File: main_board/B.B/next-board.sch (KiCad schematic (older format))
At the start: 6 parts

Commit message: preparation_to_drawing_PCB
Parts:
- removed Q?: Q_NMOS_DSG, symbol Device:Q_NMOS_DSG
- added Q?: CJ3134K, Package_TO_SOT_SMD:SOT-23, symbol Transistor_FET:2N7002
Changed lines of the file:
@@
 F3 "DIN" I L 8650 3550 50
 $EndSheet
-$Comp
-L Device:Q_NMOS_DSG Q?
-U 1 1 5FAB2954
-P 8150 3450
-AR Path="/5F9EE529/5FAB2954" Ref="Q?"  Part="1"
-AR Path="/5FA9DBB3/5FAB2954" Ref="Q?"  Part="1"
-AR Path="/5FA9675D/5FAA484F/5FAB2954" Ref="Q?"  Part="1"
-AR Path="/5FA9675D/5FAB2954" Ref="Q?"  Part="1"
-F 0 "Q?" H 8354 3496 50  0000 L CNN
-F 1 "Q_NMOS_DSG" H 8354 3405 50  0000 L CNN
-F 2 "" H 8350 3550 50  0001 C CNN
-F 3 "~" H 8150 3450 50  0001 C CNN
-	1    8150 3450
-	0    1    1    0
-$EndComp
 Text HLabel 7800 3550 0    50   Input ~ 0
 WS2812
@@
 	1    0    0    -1
 $EndComp
+$Comp
+L Transistor_FET:2N7002 Q?
+U 1 1 5FAB1240
+P 8150 3450
+AR Path="/5F77B818/5FAB1240" Ref="Q?"  Part="1"
+AR Path="/5FA9675D/5FAB1240" Ref="Q?"  Part="1"
+F 0 "Q?" H 8354 3496 50  0000 L CNN
+F 1 "CJ3134K" H 8354 3405 50  0000 L CNN
+F 2 "Package_TO_SOT_SMD:SOT-23" H 8350 3375 50  0001 L CIN
+F 3 "https://datasheet.lcsc.com/szlcsc/Changjiang-Electronics-Tech-CJ-CJ3134K_C110100.pdf" H 8150 3450 50  0001 L CNN
+F 4 "C110100" H 8150 3450 50  0001 C CNN "LCSC"
+F 5 "nutno vyměnit (musí být ->  Vgs-min>1.6V)" H 8150 3450 50  0001 C CNN "poznamka"
+	1    8150 3450
+	0    1    1    0
+$EndComp
 $EndSCHEMATC

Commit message: complete_preparation_to_drawing_PCB
footprint for all component and LCSC code for everything for mounting in JLCPCB
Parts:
- C112: renamed from C?; footprint (none) -> Capacitor_SMD:C_0402_1005Metric
- R40: renamed from R?; footprint (none) -> Resistor_SMD:R_0402_1005Metric
- gave numbers to parts that had none: 4
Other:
- moved on the sheet: C112, L3
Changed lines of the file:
@@
 $EndDescr
 $Comp
-L B.B-eagle-import:GND #GND?
+L B.B-eagle-import:GND #GND0131
 U 1 1 5FA986E8
 P 3400 4350
-F 0 "#GND?" H 3400 4350 50  0001 C CNN
+F 0 "#GND0131" H 3400 4350 50  0001 C CNN
 F 1 "GND" H 3400 4270 59  0000 C CNN
 F 2 "" H 3400 4350 50  0001 C CNN
@@
 $EndComp
 $Comp
-L B.B-eagle-import:GND #GND?
+L B.B-eagle-import:GND #GND0130
 U 1 1 5FA9899C
 P 2850 4200
-F 0 "#GND?" H 2850 4200 50  0001 C CNN
+F 0 "#GND0130" H 2850 4200 50  0001 C CNN
 F 1 "GND" H 2850 4120 59  0000 C CNN
 F 2 "" H 2850 4200 50  0001 C CNN
@@
 SHUTDOWN
 $Comp
-L B.B-rescue:LDC1314 U?
+L B.B-rescue:LDC1314 U66
 U 1 1 5FA9CA7D
 P 3400 3450
-F 0 "U?" H 3400 4325 50  0000 C CNN
+F 0 "U66" H 3400 4325 50  0000 C CNN
 F 1 "LDC1314" H 3400 4234 50  0000 C CNN
 F 2 "Package_DFN_QFN:WQFN-16-1EP_4x4mm_P0.5mm_EP2.6x2.6mm_ThermalVias" H 3400 4200 50  0001 C CNN
@@
 	8400 3550 8650 3550
 Connection ~ 8400 3550
-$Comp
-L Device:L L?
-U 1 1 60038722
-P 4200 2950
-F 0 "L?" V 4250 2850 50  0000 C CNN
-F 1 "L" V 4250 3000 50  0000 C CNN
-F 2 "" H 4200 2950 50  0001 C CNN
-F 3 "~" H 4200 2950 50  0001 C CNN
-	1    4200 2950
-	0    -1   -1   0
-$EndComp
-$Comp
-L Device:C C?
-U 1 1 6003A0BB
-P 4200 3050
-F 0 "C?" V 4150 2950 50  0000 C CNN
-F 1 "C" V 4150 3150 50  0000 C CNN
-F 2 "" H 4238 2900 50  0001 C CNN
-F 3 "~" H 4200 3050 50  0001 C CNN
-	1    4200 3050
-	0    1    1    0
-$EndComp
-Wire Wire Line
-	4000 3050 4000 2950
-Wire Wire Line
-	4000 2950 4050 2950
-Wire Wire Line
-	4000 3050 4050 3050
-Wire Wire Line
-	4350 2950 4400 2950
-Wire Wire Line
-	4400 2950 4400 3050
-Wire Wire Line
-	4400 3050 4350 3050
-Wire Wire Line
-	4400 3050 4400 3150
-Connection ~ 4400 3050
+Wire Wire Line
+	4500 3050 4500 3150
+Connection ~ 4500 3050
 Wire Wire Line
 	3900 3050 4000 3050
 Connection ~ 4000 3050
 Wire Wire Line
-	3900 3150 4400 3150
-Wire Wire Line
-	4000 3350 4000 3250
-Wire Wire Line
-	4000 3250 4050 3250
-Wire Wire Line
-	4000 3350 4050 3350
-Wire Wire Line
-	4350 3250 4400 3250
-Wire Wire Line
-	4400 3250 4400 3350
-Wire Wire Line
-	4400 3350 4350 3350
-Wire Wire Line
-	4400 3350 4400 3450
-Connection ~ 4400 3350
-Wire Wire Line
-	3900 3350 4000 3350
-Connection ~ 4000 3350
-Wire Wire Line
-	3900 3450 4400 3450
-Wire Wire Line
-	4000 3650 4000 3550
-Wire Wire Line
-	4000 3550 4050 3550
-Wire Wire Line
-	4000 3650 4050 3650
-Wire Wire Line
-	4350 3550 4400 3550
-Wire Wire Line
-	4400 3550 4400 3650
-Wire Wire Line
-	4400 3650 4350 3650
-Wire Wire Line
-	4400 3650 4400 3750
-Connection ~ 4400 3650
-Wire Wire Line
-	3900 3650 4000 3650
-Connection ~ 4000 3650
-Wire Wire Line
-	3900 3750 4400 3750
-Wire Wire Line
-	4000 3950 4000 3850
-Wire Wire Line
-	4000 3850 4050 3850
-Wire Wire Line
-	4000 3950 4050 3950
-Wire Wire Line
-	4350 3850 4400 3850
-Wire Wire Line
-	4400 3850 4400 3950
-Wire Wire Line
-	4400 3950 4350 3950
-Wire Wire Line
-	4400 3950 4400 4050
-Connection ~ 4400 3950
-Wire Wire Line
-	3900 3950 4000 3950
-Connection ~ 4000 3950
-Wire Wire Line
-	3900 4050 4400 4050
-$Comp
-L Device:R R?
+	3900 3150 4500 3150
+$Comp
+L Device:R R40
 U 1 1 60083558
 P 8400 3350
-F 0 "R?" H 8470 3396 50  0000 L CNN
+F 0 "R40" H 8470 3396 50  0000 L CNN
 F 1 "12k" H 8470 3305 50  0000 L CNN
-F 2 "" V 8330 3350 50  0001 C CNN
+F 2 "Resistor_SMD:R_0402_1005Metric" V 8330 3350 50  0001 C CNN
 F 3 "~" H 8400 3350 50  0001 C CNN
 F 4 "C25752" H 8400 3350 50  0001 C CNN "LCSC"
@@
 $EndComp
 $Comp
-L Device:R R?
+L Device:R R39
 U 1 1 5FAB4344
 P 7850 3350
-F 0 "R?" H 7920 3396 50  0000 L CNN
+F 0 "R39" H 7920 3396 50  0000 L CNN
 F 1 "12k" H 7920 3305 50  0000 L CNN
 F 2 "Resistor_SMD:R_0402_1005Metric" V 7780 3350 50  0001 C CNN
@@
 P 8150 3450
 AR Path="/5F77B818/5FAB1240" Ref="Q?"  Part="1"
-AR Path="/5FA9675D/5FAB1240" Ref="Q?"  Part="1"
-F 0 "Q?" H 8354 3496 50  0000 L CNN
+AR Path="/5FA9675D/5FAB1240" Ref="Q6"  Part="1"
+F 0 "Q6" H 8354 3496 50  0000 L CNN
 F 1 "CJ3134K" H 8354 3405 50  0000 L CNN
 F 2 "Package_TO_SOT_SMD:SOT-23" H 8350 3375 50  0001 L CIN
@@
 	0    1    1    0
 $EndComp
+Wire Wire Line
+	4500 2950 4500 3050
+Wire Wire Line
+	4000 3050 4000 2950
+Wire Wire Line
+	4450 2950 4500 2950
+Wire Wire Line
+	4000 2950 4150 2950
+$Comp
+L Device:L L3
+U 1 1 60038722
+P 4300 2950
+F 0 "L3" V 4350 2800 50  0000 C CNN
+F 1 "L" V 4350 3100 50  0000 C CNN
+F 2 "" H 4300 2950 50  0001 C CNN
+F 3 "~" H 4300 2950 50  0001 C CNN
+	1    4300 2950
+	0    -1   -1   0
+$EndComp
+Wire Wire Line
+	4000 3050 4150 3050
+Wire Wire Line
+	4500 3050 4450 3050
+$Comp
+L Device:C C112
+U 1 1 6003A0BB
+P 4300 3050
+F 0 "C112" V 4250 2900 50  0000 C CNN
+F 1 "C" V 4250 3150 50  0000 C CNN
+F 2 "Capacitor_SMD:C_0402_1005Metric" H 4338 2900 50  0001 C CNN
+F 3 "~" H 4300 3050 50  0001 C CNN
+	1    4300 3050
+	0    1    1    0
+$EndComp
+Wire Wire Line
+	3900 3350 4000 3350
+Connection ~ 4000 3350
+Wire Wire Line
+	3900 3450 4500 3450
+Wire Wire Line
+	4000 3350 4000 3250
+Wire Wire Line
+	4000 3250 4150 3250
+Wire Wire Line
+	4000 3350 4150 3350
+Wire Wire Line
+	3900 3650 4000 3650
+Connection ~ 4000 3650
+Wire Wire Line
+	3900 3750 4500 3750
+Wire Wire Line
+	4000 3650 4000 3550
+Wire Wire Line
+	4000 3550 4150 3550
+Wire Wire Line
+	4000 3650 4150 3650
+Wire Wire Line
+	3900 3950 4000 3950
+Connection ~ 4000 3950
+Wire Wire Line
+	3900 4050 4500 4050
+Wire Wire Line
+	4000 3950 4000 3850
+Wire Wire Line
+	4000 3850 4150 3850
+Wire Wire Line
+	4000 3950 4150 3950
+Wire Wire Line
+	4500 3350 4500 3450
+Connection ~ 4500 3350
+Wire Wire Line
+	4500 3250 4500 3350
+Wire Wire Line
+	4450 3250 4500 3250
+Wire Wire Line
+	4500 3350 4450 3350
+Wire Wire Line
+	4500 3650 4500 3750
+Connection ~ 4500 3650
+Wire Wire Line
+	4500 3550 4500 3650
+Wire Wire Line
+	4450 3550 4500 3550
+Wire Wire Line
+	4500 3650 4450 3650
+Wire Wire Line
+	4500 3950 4500 4050
+Connection ~ 4500 3950
+Wire Wire Line
+	4500 3850 4500 3950
+Wire Wire Line
+	4450 3850 4500 3850
+Wire Wire Line
+	4500 3950 4450 3950
 $EndSCHEMATC

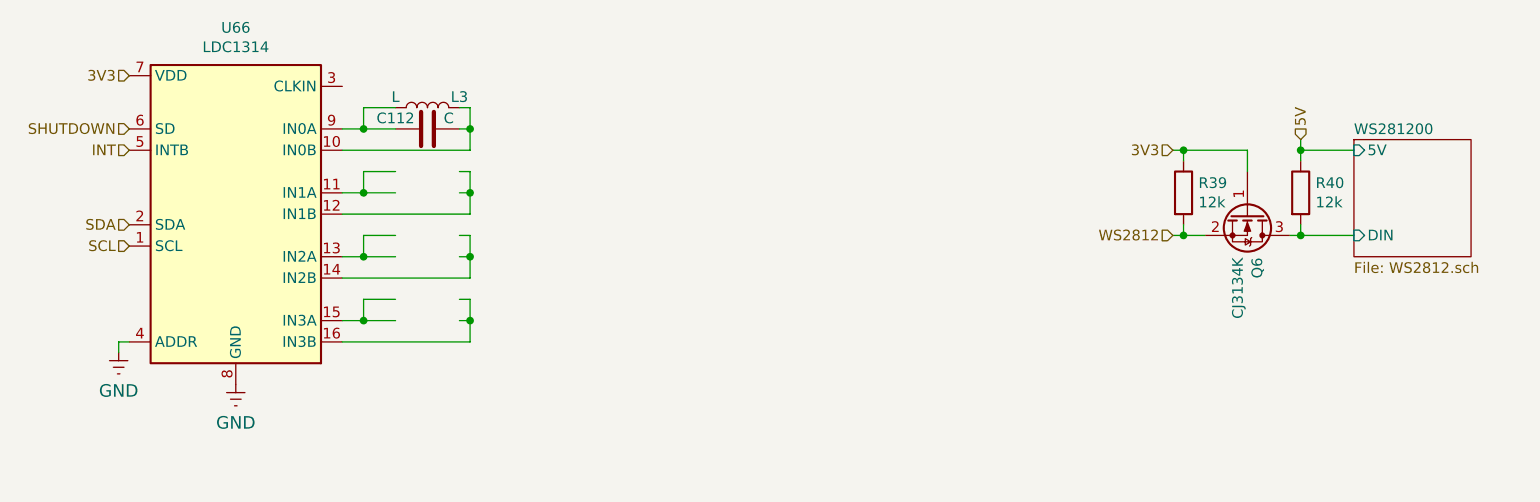
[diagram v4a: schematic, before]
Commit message: orezavani
smazaní A9G, SD karty, a zvuku
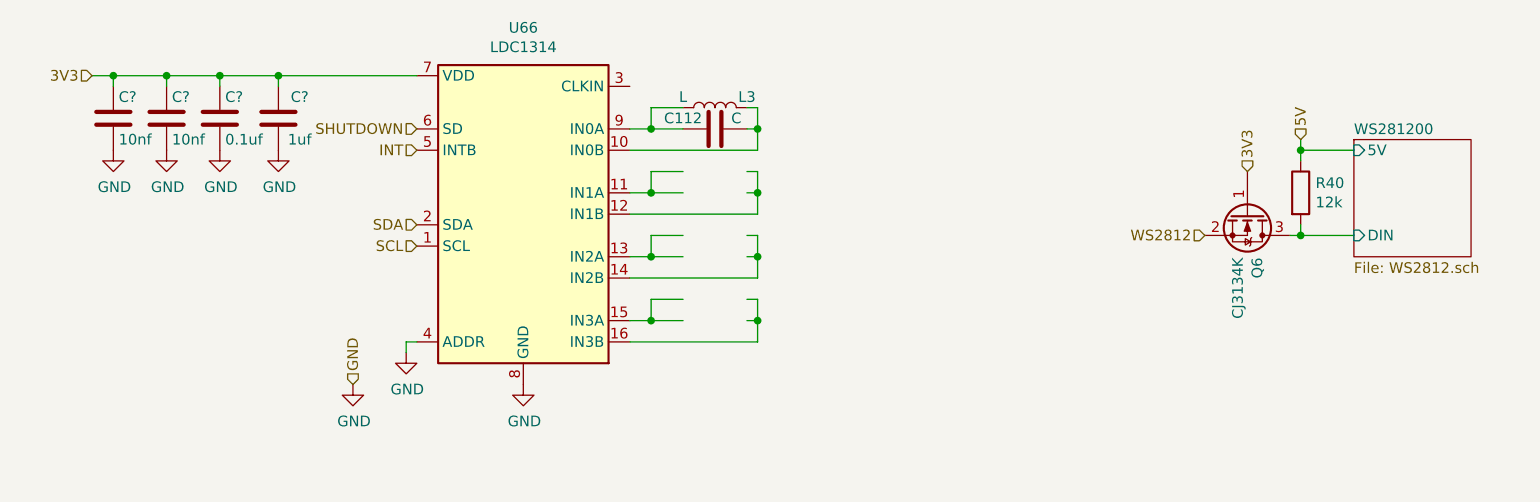
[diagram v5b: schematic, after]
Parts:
- removed R39: 12k, Resistor_SMD:R_0402_1005Metric, symbol Device:R
- added C?: 1uf, Capacitor_SMD:C_0402_1005Metric, symbol Device:C
- added C?: 0.1uf, Resistor_SMD:R_0402_1005Metric, symbol Device:C
- added C? (x2): 10nf, Capacitor_SMD:C_0402_1005Metric, symbol Device:C
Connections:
- wire segments 51 -> 53
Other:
- moved on the sheet: C112, L3, U66

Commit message: nabijecka
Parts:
- removed Q6: CJ3134K, Package_TO_SOT_SMD:SOT-23, symbol Transistor_FET:2N7002
- added Q?: 2N7002, Package_TO_SOT_SMD:SOT-23, symbol Transistor_FET:2N7002
- gave numbers to parts that had none: 4
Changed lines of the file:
@@
 $Descr A4 11693 8268
 encoding utf-8
-Sheet 3 7
+Sheet 3 8
 Title ""
 Date ""
@@
 	1    0    0    -1
 $EndComp
-$Comp
-L Transistor_FET:2N7002 Q?
-U 1 1 5FAB1240
-P 8150 3450
-AR Path="/5F77B818/5FAB1240" Ref="Q?"  Part="1"
-AR Path="/5FA9675D/5FAB1240" Ref="Q6"  Part="1"
-F 0 "Q6" H 8354 3496 50  0000 L CNN
-F 1 "CJ3134K" H 8354 3405 50  0000 L CNN
-F 2 "Package_TO_SOT_SMD:SOT-23" H 8350 3375 50  0001 L CIN
-F 3 "https://datasheet.lcsc.com/szlcsc/Changjiang-Electronics-Tech-CJ-CJ3134K_C110100.pdf" H 8150 3450 50  0001 L CNN
-F 4 "C110100" H 8150 3450 50  0001 C CNN "LCSC"
-F 5 "nutno vyměnit (musí být ->  Vgs-min>1.6V)" H 8150 3450 50  0001 C CNN "poznamka"
-	1    8150 3450
-	0    1    1    0
-$EndComp
 Wire Wire Line
 	5850 2950 5850 3050
@@
 P 4750 4250
 AR Path="/5FA9675D/5FAA484F/602204AA" Ref="#PWR?"  Part="1"
-AR Path="/5FA9675D/602204AA" Ref="#PWR?"  Part="1"
-F 0 "#PWR?" H 4750 4000 50  0001 C CNN
+AR Path="/5FA9675D/602204AA" Ref="#PWR0101"  Part="1"
+F 0 "#PWR0101" H 4750 4000 50  0001 C CNN
 F 1 "GND" H 4755 4077 50  0000 C CNN
 F 2 "" H 4750 4250 50  0001 C CNN
@@
 P 4200 4100
 AR Path="/5FA9675D/5FAA484F/60222033" Ref="#PWR?"  Part="1"
-AR Path="/5FA9675D/60222033" Ref="#PWR?"  Part="1"
-F 0 "#PWR?" H 4200 3850 50  0001 C CNN
+AR Path="/5FA9675D/60222033" Ref="#PWR0102"  Part="1"
+F 0 "#PWR0102" H 4200 3850 50  0001 C CNN
 F 1 "GND" H 4205 3927 50  0000 C CNN
 F 2 "" H 4200 4100 50  0001 C CNN
@@
 P 3950 4250
 AR Path="/5FA9675D/5FAA484F/60223B69" Ref="#PWR?"  Part="1"
-AR Path="/5FA9675D/60223B69" Ref="#PWR?"  Part="1"
-F 0 "#PWR?" H 3950 4000 50  0001 C CNN
+AR Path="/5FA9675D/60223B69" Ref="#PWR0103"  Part="1"
+F 0 "#PWR0103" H 3950 4000 50  0001 C CNN
 F 1 "GND" H 3955 4077 50  0000 C CNN
 F 2 "" H 3950 4250 50  0001 C CNN
@@
 P 3600 3000
 AR Path="/5FA4C94D/60F4C4C1" Ref="C?"  Part="1"
-AR Path="/5FA9675D/60F4C4C1" Ref="C?"  Part="1"
-F 0 "C?" H 3500 2900 50  0000 C CNN
+AR Path="/5FA9675D/60F4C4C1" Ref="C66"  Part="1"
+F 0 "C66" H 3500 2900 50  0000 C CNN
 F 1 "1uf" H 3500 3100 50  0000 C CNN
 F 2 "Capacitor_SMD:C_0402_1005Metric" H 3638 2850 50  0001 C CNN
@@
 AR Path="/5F9EE529/5FB1300F/60F4ED82" Ref="C?"  Part="1"
 AR Path="/5FB26A97/60F4ED82" Ref="C?"  Part="1"
-AR Path="/5FA9675D/60F4ED82" Ref="C?"  Part="1"
-F 0 "C?" H 3350 3100 50  0000 L CNN
+AR Path="/5FA9675D/60F4ED82" Ref="C65"  Part="1"
+F 0 "C65" H 3350 3100 50  0000 L CNN
 F 1 "0.1uf" H 3350 2900 50  0000 L CNN
 F 2 "Resistor_SMD:R_0402_1005Metric" H 3363 2850 50  0001 C CNN
@@
 AR Path="/5F9EE529/5FB1300F/60F5CF7F" Ref="C?"  Part="1"
 AR Path="/5FB26A97/60F5CF7F" Ref="C?"  Part="1"
-AR Path="/5FA9675D/60F5CF7F" Ref="C?"  Part="1"
-F 0 "C?" H 3100 3100 50  0000 L CNN
+AR Path="/5FA9675D/60F5CF7F" Ref="C64"  Part="1"
+F 0 "C64" H 3100 3100 50  0000 L CNN
 F 1 "10nf" H 3100 2900 50  0000 L CNN
 F 2 "Capacitor_SMD:C_0402_1005Metric" H 3113 2850 50  0001 C CNN
@@
 AR Path="/5F9EE529/5FB1300F/60F5DC7D" Ref="C?"  Part="1"
 AR Path="/5FB26A97/60F5DC7D" Ref="C?"  Part="1"
-AR Path="/5FA9675D/60F5DC7D" Ref="C?"  Part="1"
-F 0 "C?" H 2850 3100 50  0000 L CNN
+AR Path="/5FA9675D/60F5DC7D" Ref="C63"  Part="1"
+F 0 "C63" H 2850 3100 50  0000 L CNN
 F 1 "10nf" H 2850 2900 50  0000 L CNN
 F 2 "Capacitor_SMD:C_0402_1005Metric" H 2863 2850 50  0001 C CNN
@@
 P 2825 3150
 AR Path="/5FA9675D/5FAA484F/60F658BA" Ref="#PWR?"  Part="1"
-AR Path="/5FA9675D/60F658BA" Ref="#PWR?"  Part="1"
-F 0 "#PWR?" H 2825 2900 50  0001 C CNN
+AR Path="/5FA9675D/60F658BA" Ref="#PWR0104"  Part="1"
+F 0 "#PWR0104" H 2825 2900 50  0001 C CNN
 F 1 "GND" H 2830 2977 50  0000 C CNN
 F 2 "" H 2825 3150 50  0001 C CNN
@@
 P 3075 3150
 AR Path="/5FA9675D/5FAA484F/60F65F57" Ref="#PWR?"  Part="1"
-AR Path="/5FA9675D/60F65F57" Ref="#PWR?"  Part="1"
-F 0 "#PWR?" H 3075 2900 50  0001 C CNN
+AR Path="/5FA9675D/60F65F57" Ref="#PWR0105"  Part="1"
+F 0 "#PWR0105" H 3075 2900 50  0001 C CNN
 F 1 "GND" H 3080 2977 50  0000 C CNN
 F 2 "" H 3075 3150 50  0001 C CNN
@@
 P 3325 3150
 AR Path="/5FA9675D/5FAA484F/60F6620F" Ref="#PWR?"  Part="1"
-AR Path="/5FA9675D/60F6620F" Ref="#PWR?"  Part="1"
-F 0 "#PWR?" H 3325 2900 50  0001 C CNN
+AR Path="/5FA9675D/60F6620F" Ref="#PWR0106"  Part="1"
+F 0 "#PWR0106" H 3325 2900 50  0001 C CNN
 F 1 "GND" H 3330 2977 50  0000 C CNN
 F 2 "" H 3325 3150 50  0001 C CNN
@@
 P 3600 3150
 AR Path="/5FA9675D/5FAA484F/60F664EB" Ref="#PWR?"  Part="1"
-AR Path="/5FA9675D/60F664EB" Ref="#PWR?"  Part="1"
-F 0 "#PWR?" H 3600 2900 50  0001 C CNN
+AR Path="/5FA9675D/60F664EB" Ref="#PWR0107"  Part="1"
+F 0 "#PWR0107" H 3600 2900 50  0001 C CNN
 F 1 "GND" H 3605 2977 50  0000 C CNN
 F 2 "" H 3600 3150 50  0001 C CNN
@@
 	1    0    0    -1
 $EndComp
+$Comp
+L Transistor_FET:2N7002 Q?
+U 1 1 5FBAD606
+P 8150 3450
+AR Path="/5F77B818/5FBAD606" Ref="Q?"  Part="1"
+AR Path="/5FA4C94D/5FBAD606" Ref="Q?"  Part="1"
+AR Path="/5FA9675D/5FBAD606" Ref="Q?"  Part="1"
+F 0 "Q?" H 8354 3496 50  0000 L CNN
+F 1 "2N7002" H 8354 3405 50  0000 L CNN
+F 2 "Package_TO_SOT_SMD:SOT-23" H 8350 3375 50  0001 L CIN
+F 3 "https://datasheet.lcsc.com/szlcsc/Changjiang-Electronics-Tech-CJ-CJ3134K_C110100.pdf" H 8150 3450 50  0001 L CNN
+F 4 "C8545" H 8150 3450 50  0001 C CNN "LCSC"
+	1    8150 3450
+	0    1    1    0
+$EndComp
 $EndSCHEMATC

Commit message: 18650
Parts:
- R40: value 12k -> 7.5k; LCSC C25752 -> C25918
- gave numbers to parts that had none: 1
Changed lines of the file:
@@
 Wire Wire Line
 	5250 3150 5850 3150
-$Comp
-L Device:R R40
-U 1 1 60083558
-P 8400 3350
-F 0 "R40" H 8470 3396 50  0000 L CNN
-F 1 "12k" H 8470 3305 50  0000 L CNN
-F 2 "Resistor_SMD:R_0402_1005Metric" V 8330 3350 50  0001 C CNN
-F 3 "~" H 8400 3350 50  0001 C CNN
-F 4 "C25752" H 8400 3350 50  0001 C CNN "LCSC"
-	1    8400 3350
-	1    0    0    -1
-$EndComp
 Wire Wire Line
 	5850 2950 5850 3050
@@
 AR Path="/5F77B818/5FBAD606" Ref="Q?"  Part="1"
 AR Path="/5FA4C94D/5FBAD606" Ref="Q?"  Part="1"
-AR Path="/5FA9675D/5FBAD606" Ref="Q?"  Part="1"
-F 0 "Q?" H 8354 3496 50  0000 L CNN
+AR Path="/5FA9675D/5FBAD606" Ref="Q6"  Part="1"
+F 0 "Q6" H 8354 3496 50  0000 L CNN
 F 1 "2N7002" H 8354 3405 50  0000 L CNN
 F 2 "Package_TO_SOT_SMD:SOT-23" H 8350 3375 50  0001 L CIN
@@
 	0    1    1    0
 $EndComp
+$Comp
+L Device:R R?
+U 1 1 5FCD78C9
+P 8400 3350
+AR Path="/5FA4C94D/5FCD78C9" Ref="R?"  Part="1"
+AR Path="/5F9AAC80/5FCD78C9" Ref="R?"  Part="1"
+AR Path="/5FCD78C9" Ref="R?"  Part="1"
+AR Path="/5FA9675D/5FCD78C9" Ref="R40"  Part="1"
+F 0 "R40" V 8300 3350 50  0000 C CNN
+F 1 "7.5k" V 8500 3350 50  0000 C CNN
+F 2 "Resistor_SMD:R_0402_1005Metric" V 8330 3350 50  0001 C CNN
+F 3 "~" H 8400 3350 50  0001 C CNN
+F 4 "C25918" H 8400 3350 50  0001 C CNN "LCSC"
+	1    8400 3350
+	-1   0    0    1
+$EndComp
 $EndSCHEMATC

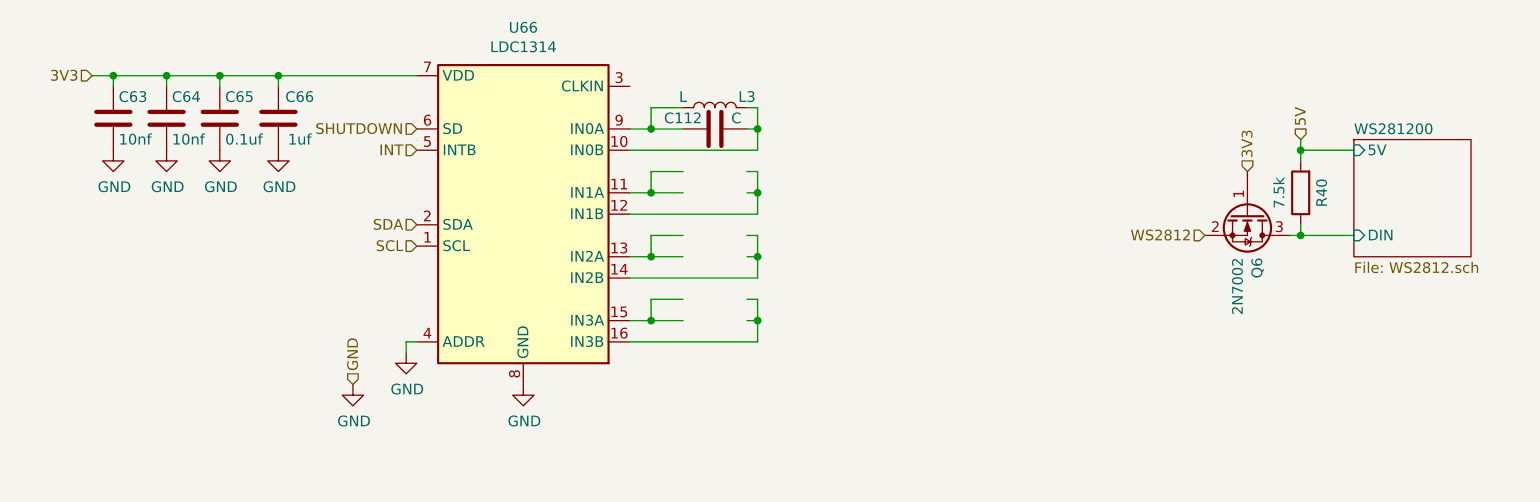
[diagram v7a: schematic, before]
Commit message: polifuse
-filtr k prijmaci IR
-merwni bterky -> za zapinani
-odstraneni odpojovani nabijecky + oprava napajeciho prouhu
-odstraneni prevodniku napeti k WS2812
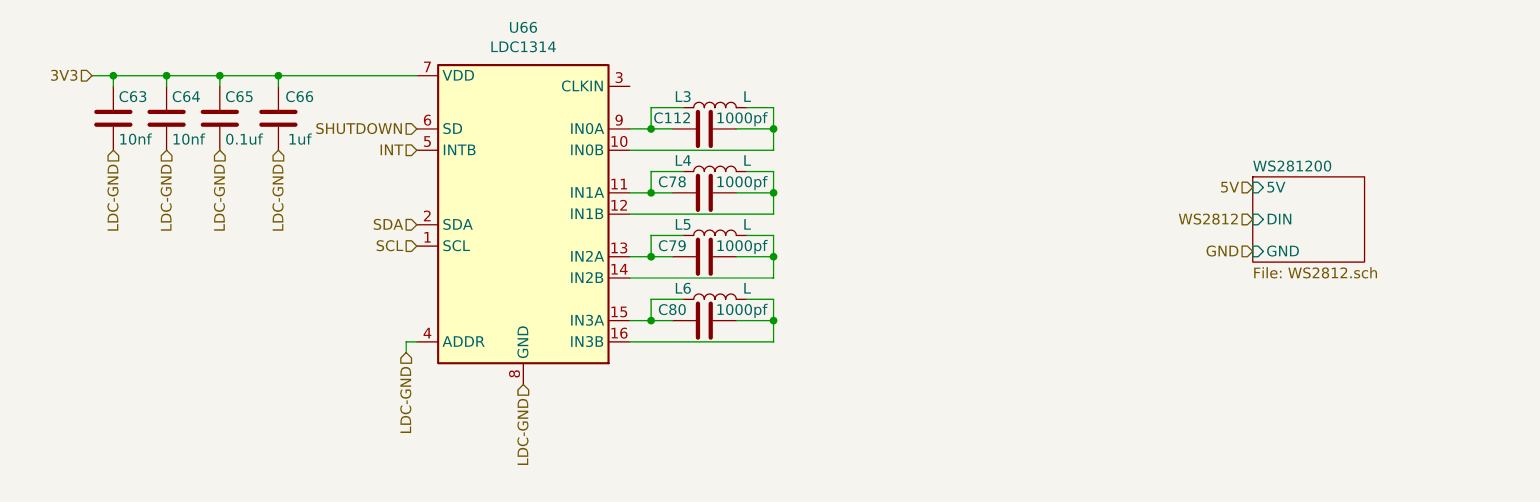
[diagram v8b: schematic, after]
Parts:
- removed Q6: 2N7002, Package_TO_SOT_SMD:SOT-23, symbol Transistor_FET:2N7002
- removed R40: 7.5k, Resistor_SMD:R_0402_1005Metric, symbol Device:R
- added C78, C79, C80: 1000pf, Capacitor_SMD:C_0402_1005Metric, symbol Device:C
- added L4, L5, L6: L, BB:coil, symbol Device:L
- C112: value C -> 1000pf
- L3: footprint (none) -> BB:coil
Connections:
- net labels added: LDC-GND
- wire segments 53 -> 47
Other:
- moved on the sheet: C112
